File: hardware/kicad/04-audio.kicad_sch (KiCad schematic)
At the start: 19 parts, among them J5 PJ-327A, Q3 2N7002, U5 PAM8403

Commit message: R36-HIGH-1 fix (v4.8.0): correct J5 headphone-jack TIP/SLEEVE swap
The v4.7.0 J5 (PJ-327A) net map was backwards on the tip/sleeve axis:
HP_L drove the sleeve and GND drove the tip, so the right headphone
channel cancelled to silence and the plug barrel sat at audio potential.
Root-caused against the HOOYA datasheet (now on disk): plug-travel
diagram + internal schematic both give pin 2 = SLEEVE, pin 3 = TIP,
pin 5 = RING, pin 6 = SLEEVE NC switch, pin 4 = TIP rest (unused).

Fix (minimal, clean re-route — only the two left-column pads move):
- pad 2 -> GND (SLEEVE), pad 3 -> HP_L (TIP); pad 5 HP_R unchanged.
- Detect KEPT on pad 6, the sleeve NC switch: with pad 2 = GND it is
  GROUND-REFERENCED when closed, so JACK_DET reads a clean 0V (no audio
  on the detect) -> R35-LOW-1 moot, no C41 gate-RC needed.
- lib_symbols: pin NUMBERS 2<->3 corrected, names -> TIP/SLV/SSW/TSW.
- datasheet_specs, footprint + primitives comments, schematic detect
  notes, and verify_polarity._strict all updated to the datasheet-true
  mapping; the map is now asserted by verify_polarity + verify_datasheet_nets
  + verify_netlist_diff (a re-swap fails all three).

Copper changed only in the J5 corner: 0 DANGER, 0 new WARN, 0 islands.
CPL/BOM unchanged (no part/rotation change) — only gerbers move.
verify-all green (200/0 incl. vbench header + gerber e-test). Set v4.8.0.
Residual (first-article): confirm speaker mutes on plug insert (pin 6 opens).

Co-Authored-By: Claude Fable 5 <noreply@anthropic.com>
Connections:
- net GND: now also J5.2 (SLV); no longer J5.3 (SLV)
- net HP_L: now also J5.3 (TIP); no longer J5.2 (TIP)
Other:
- note added: "JACK_DET high -> Q3 pulls PAM8403 MUTE low (spk off)."
- note added: "Plug inserted -> sleeve switch opens -> R40 pulls"
- note added: "Unplugged: sleeve switch ties JACK_DET to GND (0V),"
- note added: "so Q3 is hard off and the speaker plays."
- note removed: "(audio peaks < 2N7002 Vgs(th) min - no chatter)."
- note removed: "Plug inserted -> TSW opens -> R40 pulls JACK_DET"
- note removed: "Unplugged: TSW ties the gate to the tip's ~0V DC"
- note removed: "high -> Q3 pulls PAM8403 MUTE low (speaker off)."
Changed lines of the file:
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@@
   (global_label "JACK_DET" (shape output) (at 281.94 62.23 90) (effects (font (size 1.27 1.27))) (property "Intersheetrefs" "" (at 0 0 0) (effects (font (size 1.27 1.27)) hide)))
   (no_connect (at 275.59 69.85))
-  (text "Plug inserted -> TSW opens -> R40 pulls JACK_DET" (at 200 140 0) (effects (font (size 1.5 1.5)) (justify left)))
-  (text "high -> Q3 pulls PAM8403 MUTE low (speaker off)." (at 200 143.5 0) (effects (font (size 1.5 1.5)) (justify left)))
-  (text "Unplugged: TSW ties the gate to the tip's ~0V DC" (at 200 147 0) (effects (font (size 1.5 1.5)) (justify left)))
-  (text "(audio peaks < 2N7002 Vgs(th) min - no chatter)." (at 200 150.5 0) (effects (font (size 1.5 1.5)) (justify left)))
+  (text "Plug inserted -> sleeve switch opens -> R40 pulls" (at 200 140 0) (effects (font (size 1.5 1.5)) (justify left)))
+  (text "JACK_DET high -> Q3 pulls PAM8403 MUTE low (spk off)." (at 200 143.5 0) (effects (font (size 1.5 1.5)) (justify left)))
+  (text "Unplugged: sleeve switch ties JACK_DET to GND (0V)," (at 200 147 0) (effects (font (size 1.5 1.5)) (justify left)))
+  (text "so Q3 is hard off and the speaker plays." (at 200 150.5 0) (effects (font (size 1.5 1.5)) (justify left)))
   (symbol (lib_id "emu:R") (at 226.06 118.11 0) (unit 1) (exclude_from_sim no) (in_bom yes) (on_board yes) (dnp no) (property "Reference" "R40" (at 228.18 116.31 0) (effects (font (size 1.27 1.27)) (justify left))) (property "Value" "220k" (at 228.18 119.91 0) (effects (font (size 1.27 1.27)) (justify left))) (pin "1") (pin "2") (instances (project "esp32-emu-turbo" (path "/00000005-cafe-4000-8000-000000000005" (reference "R40") (unit 1)) (path "/00000001-cafe-4000-8000-000000000001/00000005-cafe-4000-8000-000000000005" (reference "R40") (unit 1)))))
   (symbol (lib_id "emu:+3V3") (at 226.06 111.76 0) (unit 1) (exclude_from_sim no) (in_bom no) (on_board no) (dnp no) (property "Reference" "#PWR009" (at 226.06 109.76 0) (effects (font (size 1.27 1.27)) hide)) (property "Value" "+3V3" (at 226.06 113.76 0) (effects (font (size 1.27 1.27)) hide)) (pin "1") (instances (project "esp32-emu-turbo" (path "/00000005-cafe-4000-8000-000000000005" (reference "#PWR009") (unit 1)) (path "/00000001-cafe-4000-8000-000000000001/00000005-cafe-4000-8000-000000000005" (reference "#PWR009") (unit 1)))))

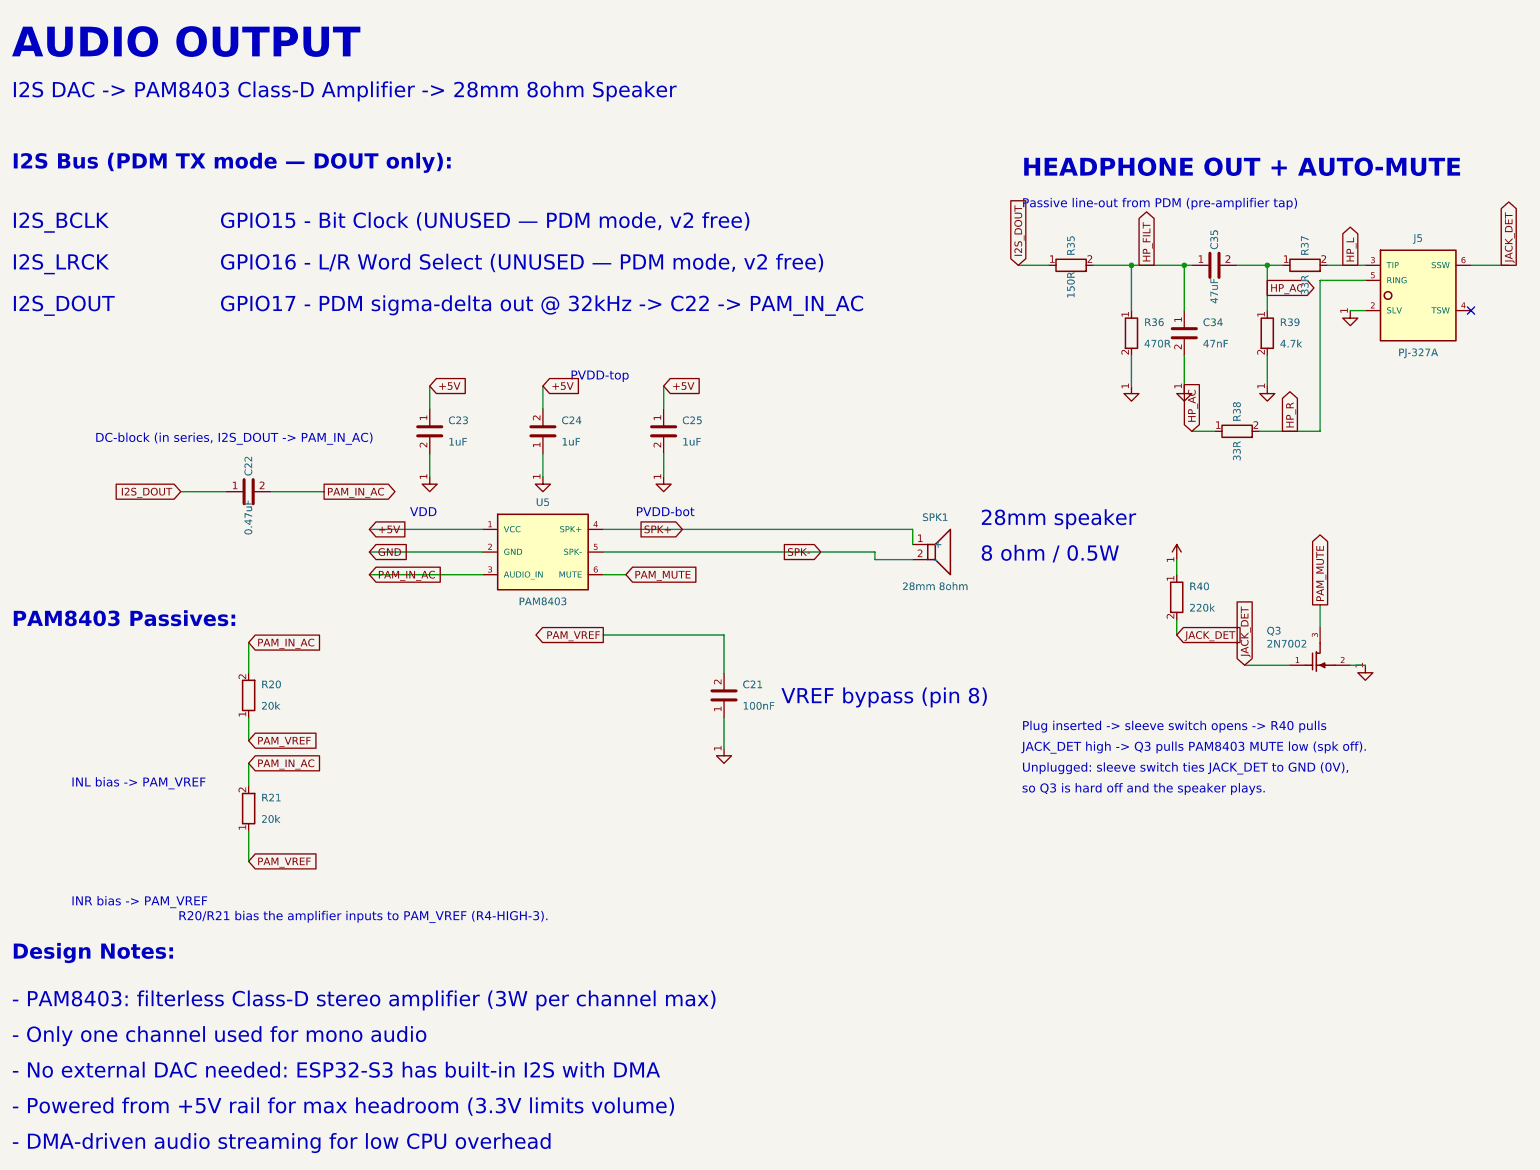
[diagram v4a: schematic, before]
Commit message: revert active design to v4.6.2 — drop the headphone jack (no-jack board)
User decision: return to the v4.6.2 board (last pre-jack design, already
ordered + phase-A validated) instead of chasing JLC SMT-DFM advisory
flags. This reverts the entire jack programme — v4.7.0 (J5 3.5mm jack +
Q3 speaker auto-mute), v4.8.0 (R36-HIGH-1 J5 TIP/SLEEVE fix) and v4.8.1
(R37 U5 land match) — back to exactly the v4.6.2 tree.

Why: the SMT-DFM "dangers" (U5/J4 pin-edge, J1 USB-C pin-without-pad,
collisions) are JLC library 3D-MODEL artifacts, not board defects — proven
the hard way in v4.8.1, where growing U5's land to match JLC's OWN
reference land exactly (coverage 1.000) still left the 73 pin-edge flags,
because JLC's 3D model lead extends ~0.08mm past their own reference land.
No IPC-compliant footprint can clear them; the copper is 0-danger and every
gate is green. Removing the jack does NOT remove these flags (they live on
USB-C/amp/FPC, not the jack) — this is purely a decision to drop the jack
FEATURE and its added risk surface, not a fix for the flags.

Board is now byte-identical to the v4.6.2 tag. Kept (non-jack, board-
independent):
- .claude/skills/jlcdfm-upload/SKILL.md — reverse-engineered JLCDFM
  upload + SMT/viewer flow (reusable tooling, no board impact)
- release_jlcpcb/jlcdfm/*.md — this session's JLCDFM reports (reference)
- scripts/verify_cpl_rotation_law.py — the LED2-6 rotation-law exception
  (R33-MED-2), which v4.6.2's own LED 0deg emit needs to pass verify-all;
  the Q3 (jack) exception from the same commit was dropped.

The v4.8.1 tag preserves the full jack design if it is ever wanted back.
Verification: verify-all 104/104 on this tree.

Co-Authored-By: Claude Opus 4.8 <noreply@anthropic.com>
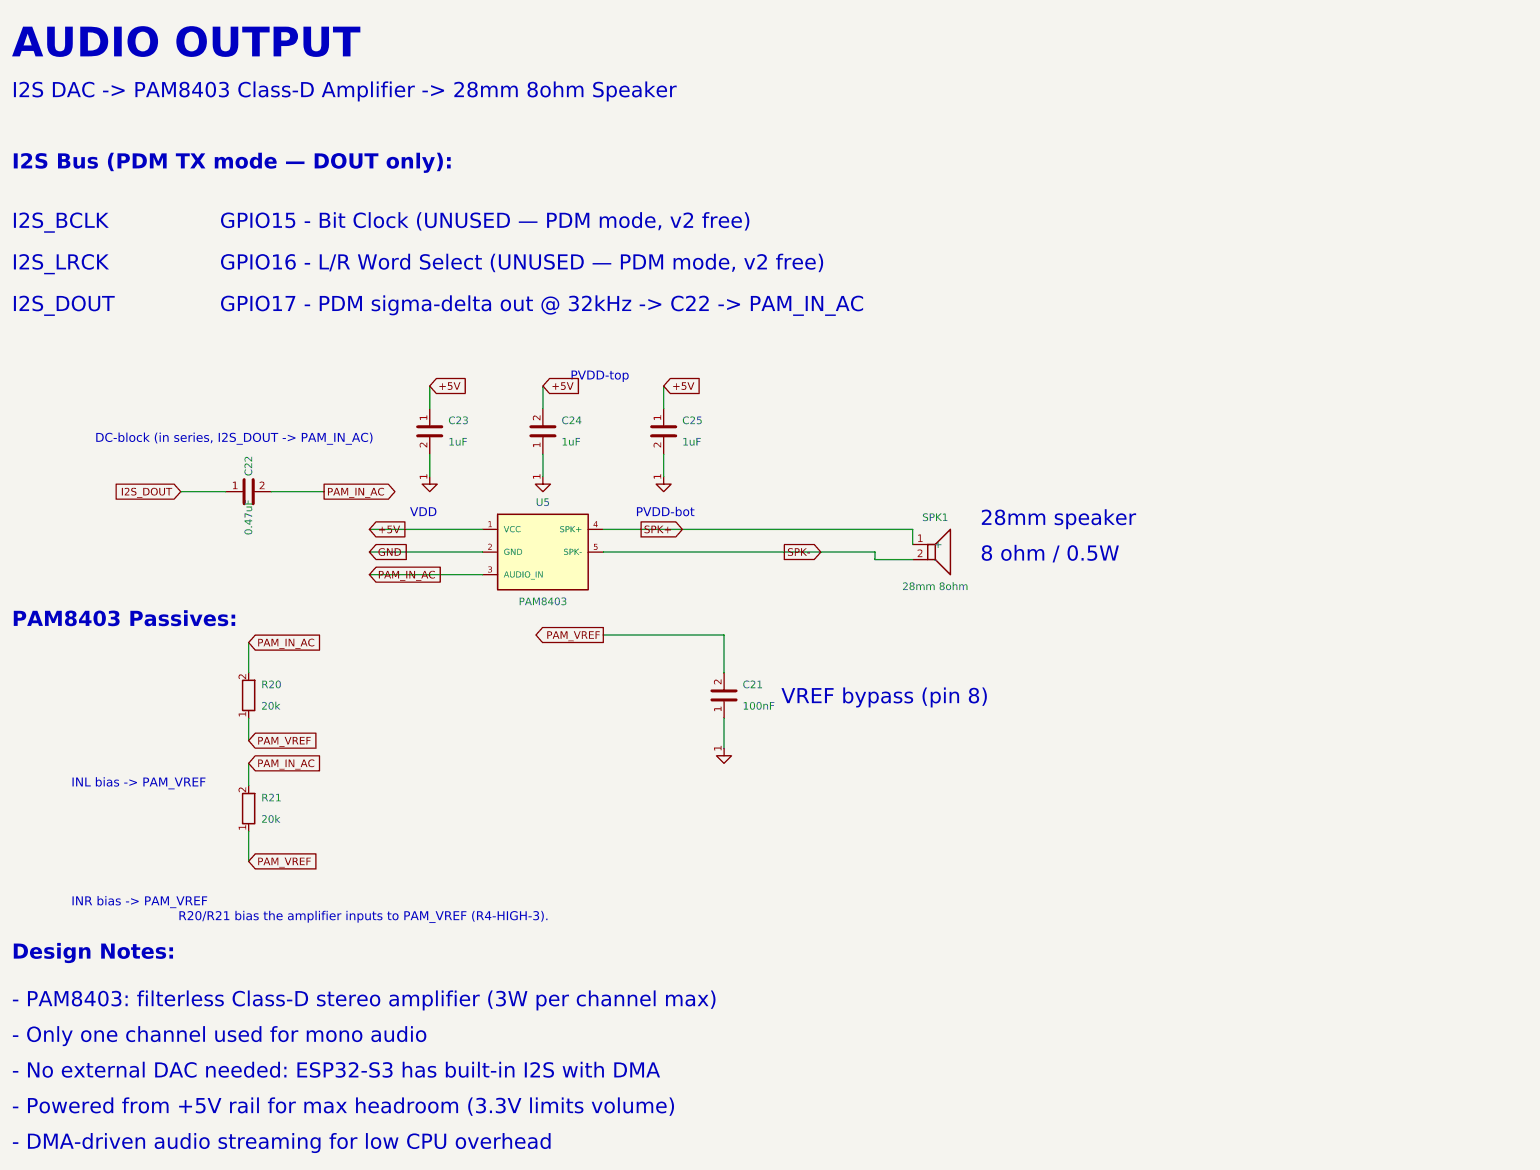
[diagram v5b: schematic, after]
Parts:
- removed C34: 47nF, symbol emu:C
- removed C35: 47uF, symbol emu:C
- removed J5: PJ-327A, symbol emu:AudioJack_PJ327A
- removed Q3: 2N7002, symbol emu:NMOS_SOT23
- removed R35: 150R, symbol emu:R
- removed R36: 470R, symbol emu:R
- removed R37, R38: 33R, symbol emu:R
- removed R39: 4.7k, symbol emu:R
- removed R40: 220k, symbol emu:R
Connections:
- removed net PAM_MUTE: U5.6 (MUTE)
- no-connect marks 1 -> 0
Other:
- note removed: "HEADPHONE OUT + AUTO-MUTE"
- note removed: "JACK_DET high -> Q3 pulls PAM8403 MUTE low (spk off)."
- note removed: "Passive line-out from PDM (pre-amplifier tap)"
- note removed: "Plug inserted -> sleeve switch opens -> R40 pulls"
- note removed: "Unplugged: sleeve switch ties JACK_DET to GND (0V),"
- note removed: "so Q3 is hard off and the speaker plays."
- title: Audio - I2S -> PAM8403 -> Speaker + Headphone Jack -> Audio - I2S -> PAM8403 -> Speaker
